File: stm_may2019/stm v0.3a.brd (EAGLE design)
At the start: 128.9 x 105.8 mm, 140 parts, among them Q1 MMBT3906, Q2 MMBT3904, Q3 MMBT3904, Y1 32.768kHz

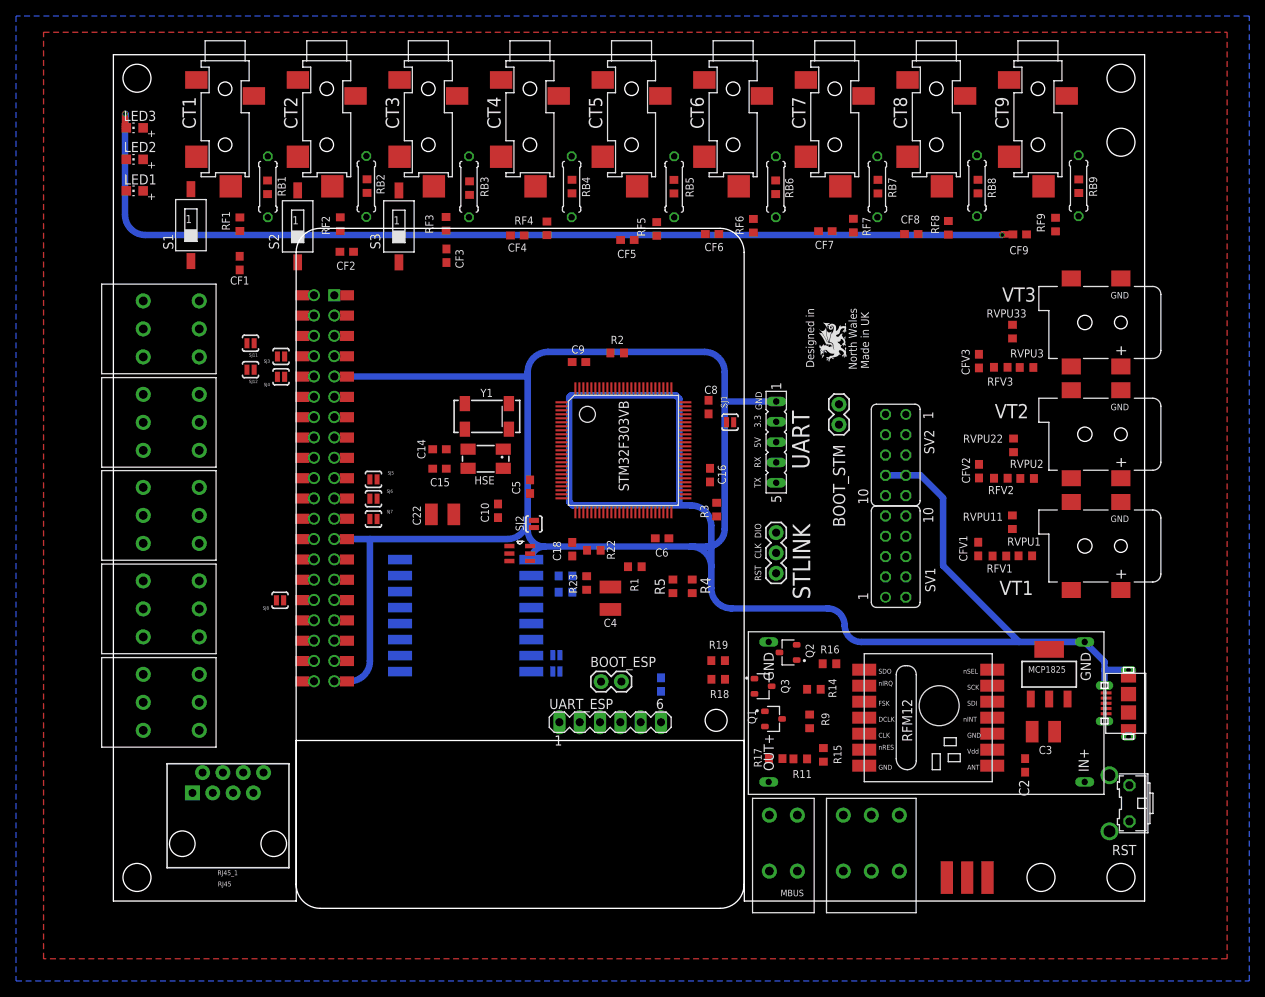
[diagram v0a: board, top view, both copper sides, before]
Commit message: v0.3a and gerbers
also includes prelim cubeMX project
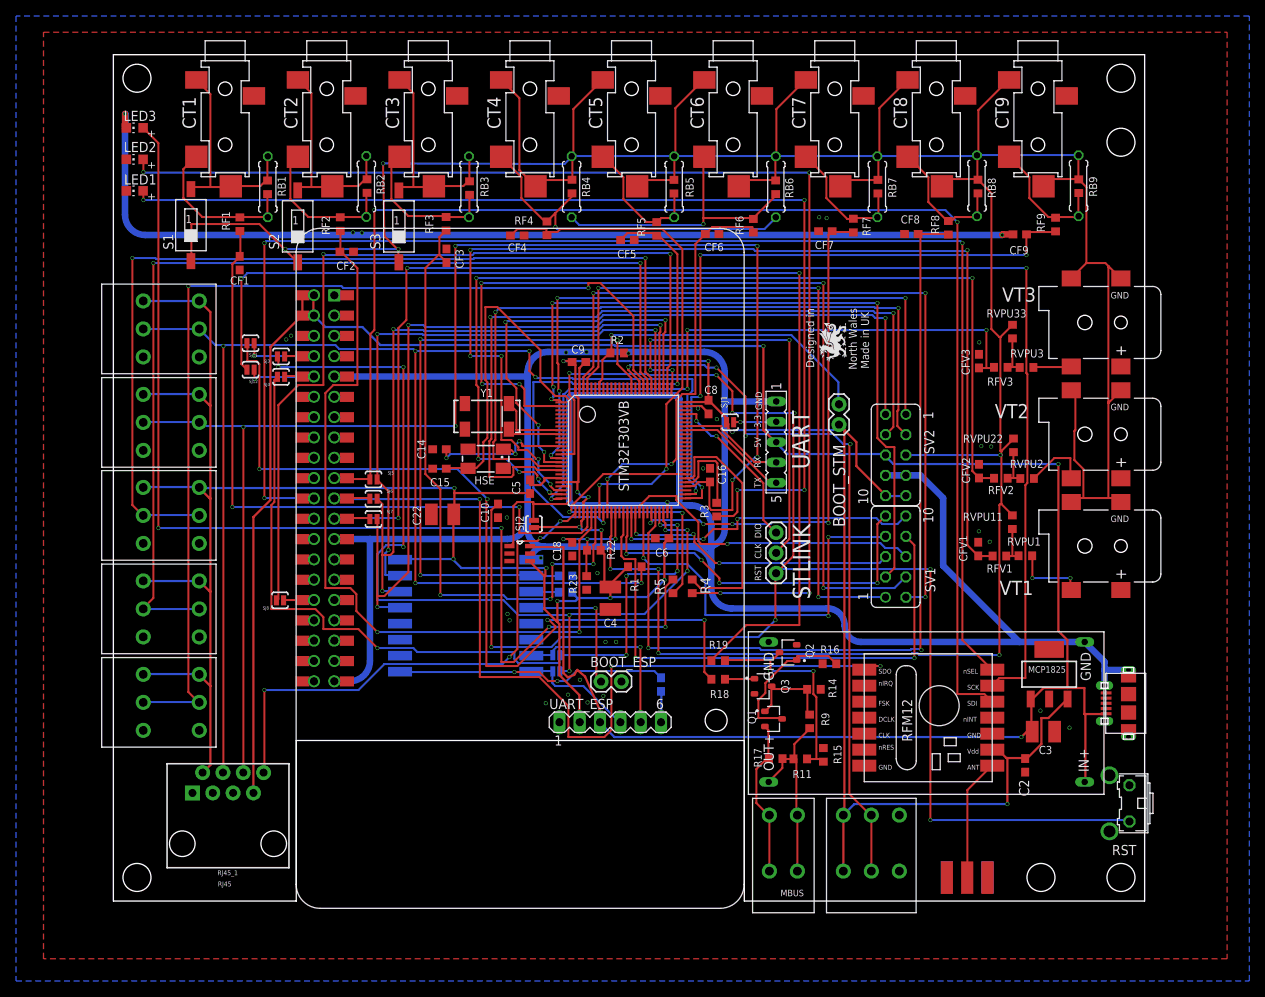
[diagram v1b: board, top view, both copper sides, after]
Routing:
- net BIAS: track 0.00 -> 470.9 mm, vias 0 -> 8
- net +3V3: track 0.00 -> 426.2 mm, vias 0 -> 14
- net +5V: track 0.00 -> 315.4 mm, vias 0 -> 3
- net DS18B20: track 0.00 -> 202.0 mm, vias 0 -> 7
- net NRST: track 0.00 -> 201.7 mm, vias 0 -> 8
- net PULSE: track 0.00 -> 186.9 mm, vias 0 -> 6
- net CS_RFM69: track 0.00 -> 182.0 mm, vias 0 -> 3
- net SPI_CLK: track 0.00 -> 177.9 mm, vias 0 -> 3
- net MOSI: track 0.00 -> 175.7 mm, vias 0 -> 2
- net N$5: track 0.00 -> 152.1 mm, vias 0 -> 4
- net VSIG1: track 0.00 -> 142.0 mm, vias 0 -> 6
- net N$6: track 0.00 -> 139.1 mm, vias 0 -> 4
- net MBUS_TX: track 0.00 -> 138.6 mm, vias 0 -> 2
- net N$41: track 0.00 -> 134.0 mm, vias 0 -> 4
- net PUSHIN_4: track 0.00 -> 127.7 mm, vias 0 -> 2
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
